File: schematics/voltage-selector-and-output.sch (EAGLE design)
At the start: 22 parts, among them IC1 3.3V, IC2 MIC2941, IC4 ULN2003AN, IC6 ATTINY85, IC7 74LS595N

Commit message: Finally updated the primary schematic
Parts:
- removed INPUT: (no value), SparkFun:M02PTH
- removed ISP1: AVRISP-6, adafruit:AVRISP-6
- removed JP1: (no value), SparkFun:M02JST-PTH-2
- removed R11: 10k, rcl-ez:R-US_0207/5V
- removed R7: 11k, rcl-ez:R-US_0207/5V
- removed R8: 20.5k, rcl-ez:R-US_0207/5V
- removed R9: 41.2k, rcl-ez:R-US_0207/5V
- removed R97: 6.49K 1%, rcl-ez:R-US_0207/5V
- added C1, C4: 47uF/25V, minimidi:CPOL-USE2.5-6
- added C5: 0.1uF, SparkFun-Capacitors:CAPPTH
- added D1, D2, D3, D4: 1N4007, gm-diodes:1N400X.3
- added D6: (no value), SparkFun-LED:LED-3MM-NO_SILK
- added IC3: MCP41010P, microchip-custom:MCP41010P
- added IC5: 12V, v-reg:78XXS
- added ISP: AVRISP-6, adafruit:AVRISP-6
- added JACK, XFRM: (no value), SparkFun:M02PTH
- added R2: 10k, rcl-ez:R-US_0207/5V
- added R3: 1K, rcl-ez:R-US_0207/5V
- added R4: 470, SparkFun-Resistors:RESISTORPTH-1/4W
- added TOGGLE: SPST, gm-switches:SPST
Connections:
- net N$17 renamed PB4
- removed net ISP_VCC: IC1.OUT, IC6.VCC, ISP1.VCC, JP4.1
- removed net N$15: IC6.PB5(NRES), ISP1.RST
- removed net N$16: IC6.PB3(ADC3), IC7A.SCK
- removed net N$18: IC6.PB2(SCK/ADC1), IC7A.RCK, ISP1.SCK
- removed net N$19: IC6.PB0(MOSI), ISP1.MOSI, JP4.2, R1.2
- removed net N$22: IC4.O1, R7.2
- removed net N$23: IC6.PB1(MISO), IC7A.SER, ISP1.MISO
- removed net N$24: IC4.O2, R8.2
- removed net N$25: IC4.O3, R9.2
- removed net N$8: IC2.ADJ, POT.2, R97.2
- new net IC_VCC: IC1.OUT, IC3.PA0, IC3.VDD, IC6.VCC, ISP.VCC, JP4.1
- new net N$2: D1.A, D3.C, XFRM.2
- new net N$3: D2.A, D4.C, XFRM.1
- new net N$4: IC2.ADJ, IC3.PW0, R3.2
- new net N$5: D6.C, R4.2
- new net N$6: POT.2
- new net N$9: C4.+, D1.C, D2.C, TOGGLE.P
- new net PB0: IC6.PB0(MOSI), ISP.MOSI, JP4.2, R1.2
- new net PB1: IC3.SI, IC6.PB1(MISO), IC7A.SER, ISP.RST
- new net PB2: IC3.SCK, IC6.PB2(SCK/ADC1), IC7A.RCK, ISP.SCK
- new net PB3: IC3./CS, IC6.PB3(ADC3), IC7A.SCK
- new net PB5: IC6.PB5(NRES), ISP.MISO
- new net RECTIFIED_12VCC: C1.+, C5.1, D6.A, IC1.IN, IC2.IN, IC5.OUT
- net AGND: now also C1.-, C4.-, C5.2, D3.A, D4.A, IC3.PB0, IC3.VSS, IC5.GND, ISP.GND, JACK.2, R2.2, R3.1, R4.1; no longer IC4.GND, INPUT.1, ISP1.GND, R11.2, R97.1
- net N$1: now also IC5.IN, TOGGLE.S; no longer IC1.IN, IC2.IN, INPUT.2
- net N$27: no longer IC4.I1
- net N$28: no longer IC4.I2
- net N$29: no longer IC4.I3
- net N$30: no longer IC4.I4
- net N$31: no longer IC4.I5
- net N$34: now also R2.1; no longer R11.1
- net VADJ: now also JACK.1
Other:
- moved on the sheet: IC1, IC4, IC6, IC7, JP4, METER, POSTS, POT, R1, SOCKET, USB

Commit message: Changed the pin being used for the pot SI
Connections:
- net PB1: no longer IC3.SI
- net PB5: now also IC3.SI
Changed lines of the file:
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@@
 <label x="33.02" y="83.82" size="1.778" layer="95"/>
+</segment>
+<segment>
+<pinref part="IC3" gate="P1" pin="SI"/>
+<wire x1="43.18" y1="139.7" x2="45.72" y2="139.7" width="0.1524" layer="91"/>
+<label x="45.72" y="139.7" size="1.778" layer="95"/>
 </segment>
 </net>
@@
 <label x="58.42" y="104.14" size="1.778" layer="95"/>
 </segment>
-<segment>
-<pinref part="IC3" gate="P1" pin="SI"/>
-<wire x1="43.18" y1="139.7" x2="45.72" y2="139.7" width="0.1524" layer="91"/>
-<label x="45.72" y="139.7" size="1.778" layer="95"/>
-</segment>
 </net>

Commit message: Resized board boundary to what I have room for and removed transistor array
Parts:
- removed IC4: ULN2003AN, uln-udn:ULN2003AN
- added Q1: 2N3906, transistor-pnp:2N3906
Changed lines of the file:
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@@
 <part name="GND8" library="supply1" deviceset="AGND" device="" value="GND"/>
 <part name="JP4" library="SparkFun" deviceset="M08" device="1X08"/>
-<part name="IC4" library="uln-udn" deviceset="ULN2003A" device="N"/>
 <part name="GND7" library="supply1" deviceset="AGND" device="" value="GND"/>
 <part name="IC7" library="74xx-us" deviceset="74*595" device="N" technology="LS"/>
@@
 <part name="C5" library="SparkFun-Capacitors" deviceset="CAP" device="PTH" value="0.1uF"/>
 <part name="JACK" library="SparkFun" deviceset="M02" device="PTH"/>
+<part name="Q1" library="transistor-pnp" deviceset="2N3906" device=""/>
 </parts>
 <sheets>
@@
 <instance part="GND8" gate="VR1" x="40.64" y="111.76" rot="R180"/>
 <instance part="JP4" gate="G$1" x="106.68" y="93.98" rot="MR0"/>
-<instance part="IC4" gate="A" x="124.46" y="213.36" rot="MR0"/>
 <instance part="GND7" gate="VR1" x="101.6" y="106.68" rot="MR180"/>
 <instance part="IC7" gate="A" x="73.66" y="93.98"/>
@@
 <instance part="C5" gate="G$1" x="88.9" y="223.52"/>
 <instance part="JACK" gate="G$1" x="132.08" y="134.62" rot="R180"/>
+<instance part="Q1" gate="G$1" x="78.74" y="119.38"/>
 </instances>
 <busses>

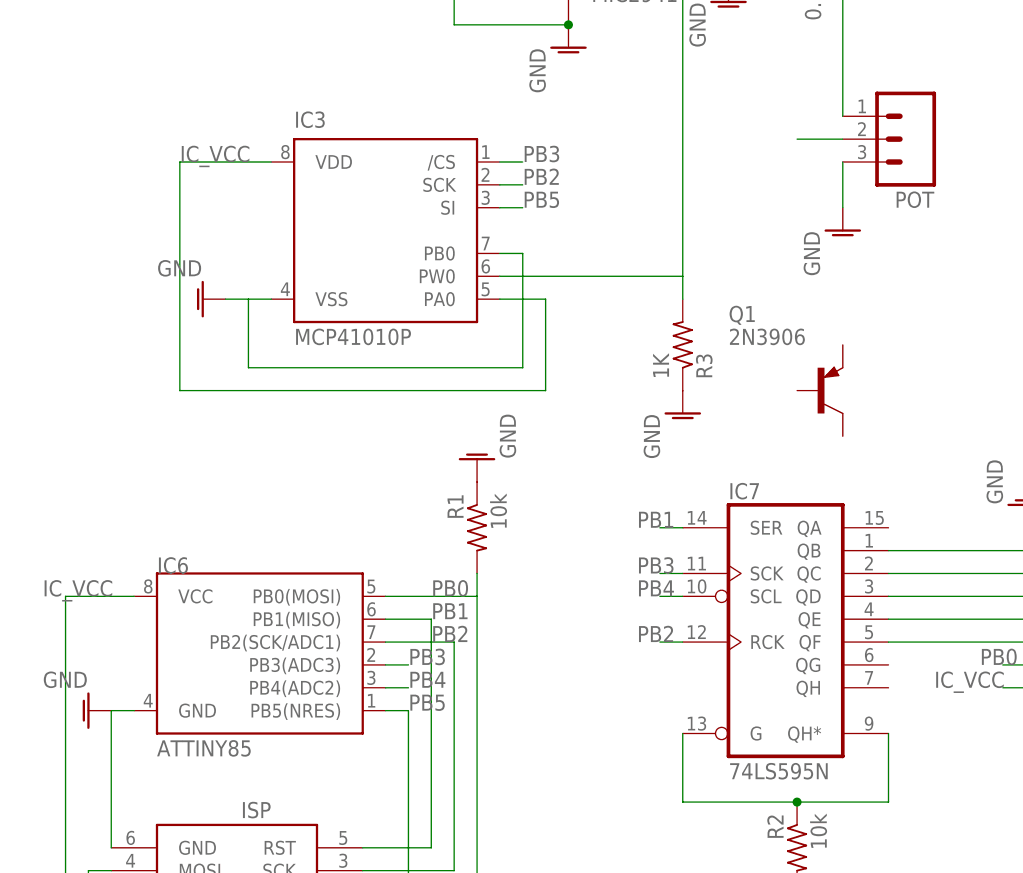
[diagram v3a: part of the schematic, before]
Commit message: Finally got to working on the main board layout
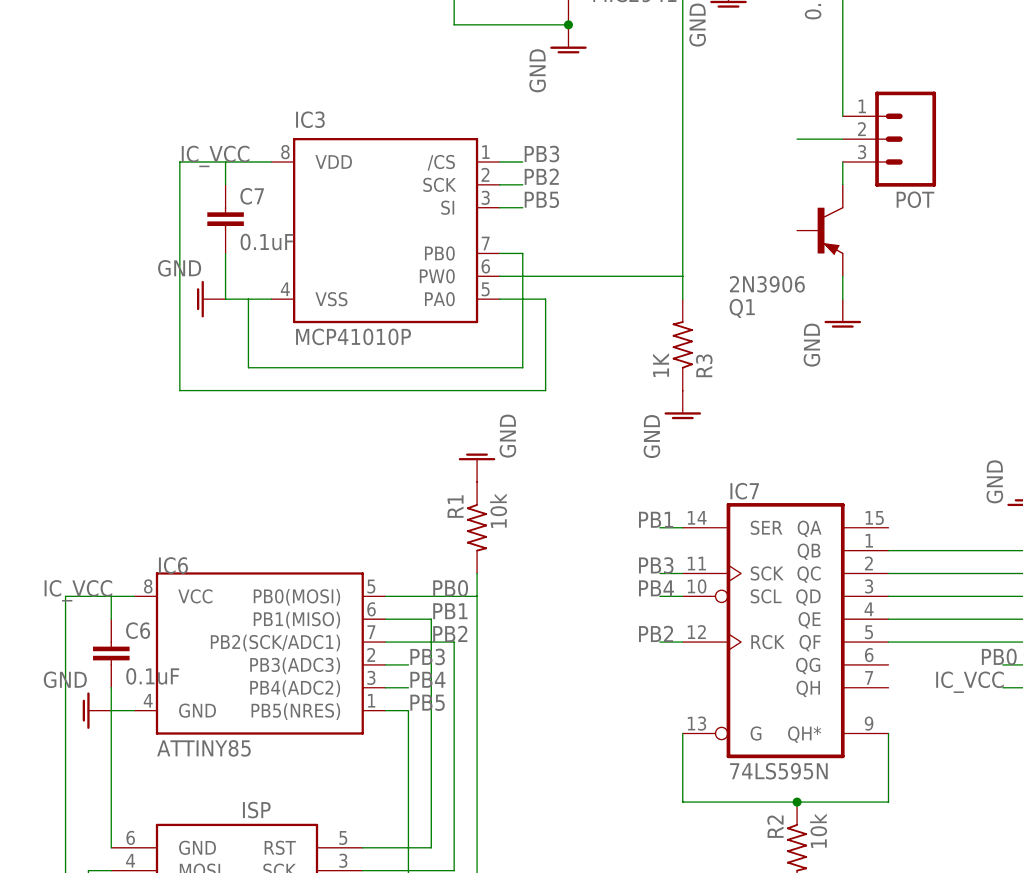
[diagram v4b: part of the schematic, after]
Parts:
- added C6, C7: 0.1uF, SparkFun-Capacitors:CAPPTH
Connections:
- new net N$7: POT.3, Q1.C
- net AGND: now also C6.2, C7.2, Q1.E; no longer POT.3
- net IC_VCC: now also C6.1, C7.1
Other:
- moved on the sheet: Q1
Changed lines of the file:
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@@
 <part name="JACK" library="SparkFun" deviceset="M02" device="PTH"/>
 <part name="Q1" library="transistor-pnp" deviceset="2N3906" device=""/>
+<part name="C6" library="SparkFun-Capacitors" deviceset="CAP" device="PTH" value="0.1uF"/>
+<part name="C7" library="SparkFun-Capacitors" deviceset="CAP" device="PTH" value="0.1uF"/>
 </parts>
 <sheets>
@@
 <instance part="USB" gate="G$1" x="132.08" y="172.72" rot="R180"/>
 <instance part="POT" gate="G$1" x="88.9" y="147.32" rot="R180"/>
-<instance part="GND11" gate="VR1" x="81.28" y="137.16"/>
+<instance part="GND11" gate="VR1" x="81.28" y="127"/>
 <instance part="IC3" gate="P1" x="30.48" y="137.16"/>
 <instance part="ISP" gate="G$1" x="15.24" y="66.04" rot="R180"/>
@@
 <instance part="C5" gate="G$1" x="88.9" y="223.52"/>
 <instance part="JACK" gate="G$1" x="132.08" y="134.62" rot="R180"/>
-<instance part="Q1" gate="G$1" x="78.74" y="119.38"/>
+<instance part="Q1" gate="G$1" x="78.74" y="137.16" rot="MR180"/>
+<instance part="C6" gate="G$1" x="0" y="88.9"/>
+<instance part="C7" gate="G$1" x="12.7" y="137.16"/>
 </instances>
 <busses>
@@
 <wire x1="0" y1="63.5" x2="-5.08" y2="63.5" width="0.1524" layer="91"/>
 <wire x1="-5.08" y1="63.5" x2="-5.08" y2="96.52" width="0.1524" layer="91"/>
-<wire x1="-5.08" y1="96.52" x2="2.54" y2="96.52" width="0.1524" layer="91"/>
+<wire x1="-5.08" y1="96.52" x2="0" y2="96.52" width="0.1524" layer="91"/>
+<pinref part="C6" gate="G$1" pin="1"/>
+<wire x1="0" y1="96.52" x2="2.54" y2="96.52" width="0.1524" layer="91"/>
+<wire x1="0" y1="93.98" x2="0" y2="96.52" width="0.1524" layer="91"/>
 </segment>
 <segment>
@@
 <wire x1="7.62" y1="119.38" x2="7.62" y2="144.78" width="0.1524" layer="91"/>
 <pinref part="IC3" gate="P1" pin="VDD"/>
-<wire x1="7.62" y1="144.78" x2="17.78" y2="144.78" width="0.1524" layer="91"/>
+<wire x1="7.62" y1="144.78" x2="12.7" y2="144.78" width="0.1524" layer="91"/>
 <label x="7.62" y="144.78" size="1.778" layer="95"/>
+<pinref part="C7" gate="G$1" pin="1"/>
+<wire x1="12.7" y1="144.78" x2="17.78" y2="144.78" width="0.1524" layer="91"/>
+<wire x1="12.7" y1="142.24" x2="12.7" y2="144.78" width="0.1524" layer="91"/>
 </segment>
 </net>
@@
 </segment>
 <segment>
-<pinref part="POT" gate="G$1" pin="3"/>
 <pinref part="GND11" gate="VR1" pin="AGND"/>
-<wire x1="81.28" y1="144.78" x2="81.28" y2="139.7" width="0.1524" layer="91"/>
+<pinref part="Q1" gate="G$1" pin="E"/>
+<wire x1="81.28" y1="132.08" x2="81.28" y2="129.54" width="0.1524" layer="91"/>
 </segment>
 <segment>
@@
 <wire x1="45.72" y1="121.92" x2="15.24" y2="121.92" width="0.1524" layer="91"/>
 <wire x1="15.24" y1="121.92" x2="15.24" y2="129.54" width="0.1524" layer="91"/>
+<pinref part="C7" gate="G$1" pin="2"/>
+<wire x1="12.7" y1="134.62" x2="12.7" y2="129.54" width="0.1524" layer="91"/>
 </segment>
 <segment>
@@
 <wire x1="0" y1="83.82" x2="2.54" y2="83.82" width="0.1524" layer="91"/>
 <wire x1="0" y1="68.58" x2="0" y2="83.82" width="0.1524" layer="91"/>
+<pinref part="C6" gate="G$1" pin="2"/>
+<wire x1="0" y1="86.36" x2="0" y2="83.82" width="0.1524" layer="91"/>
 </segment>
 <segment>
@@
 </segment>
 </net>
+<net name="N$7" class="0">
+<segment>
+<pinref part="POT" gate="G$1" pin="3"/>
+<wire x1="81.28" y1="144.78" x2="81.28" y2="142.24" width="0.1524" layer="91"/>
+<pinref part="Q1" gate="G$1" pin="C"/>
+</segment>
+</net>

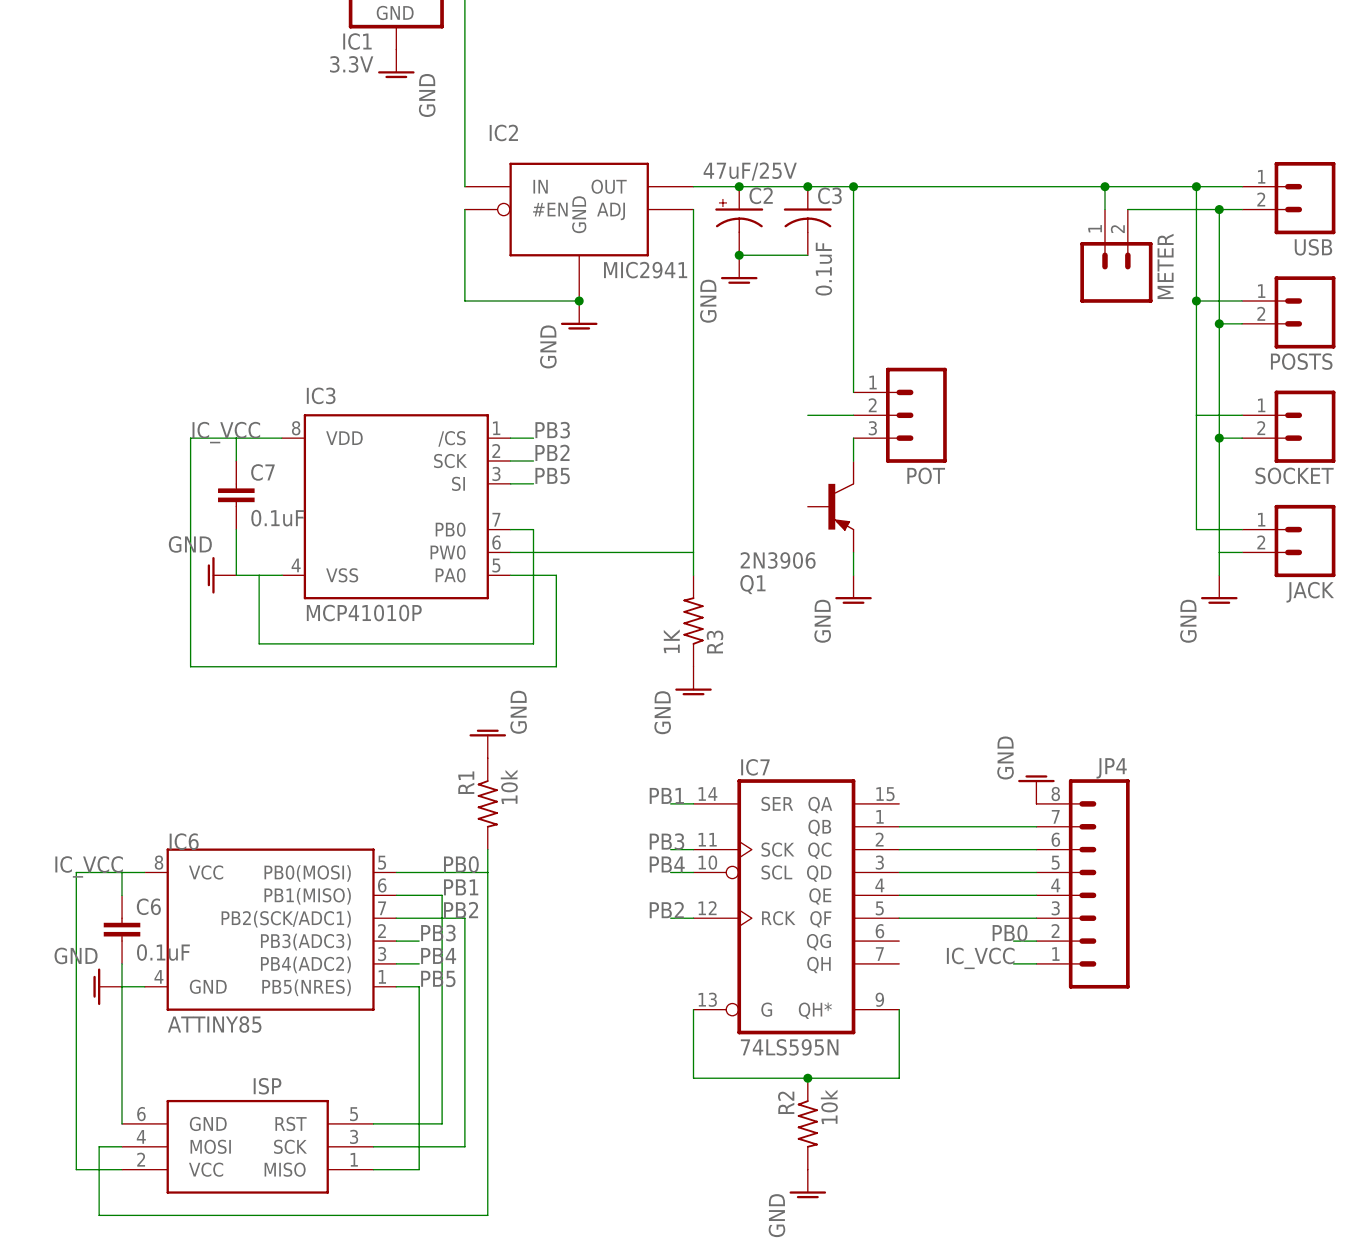
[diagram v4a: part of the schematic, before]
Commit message: Moved the shift register to the top board since I have more room there and on the bottom board and I get to free up some pins on the jumper
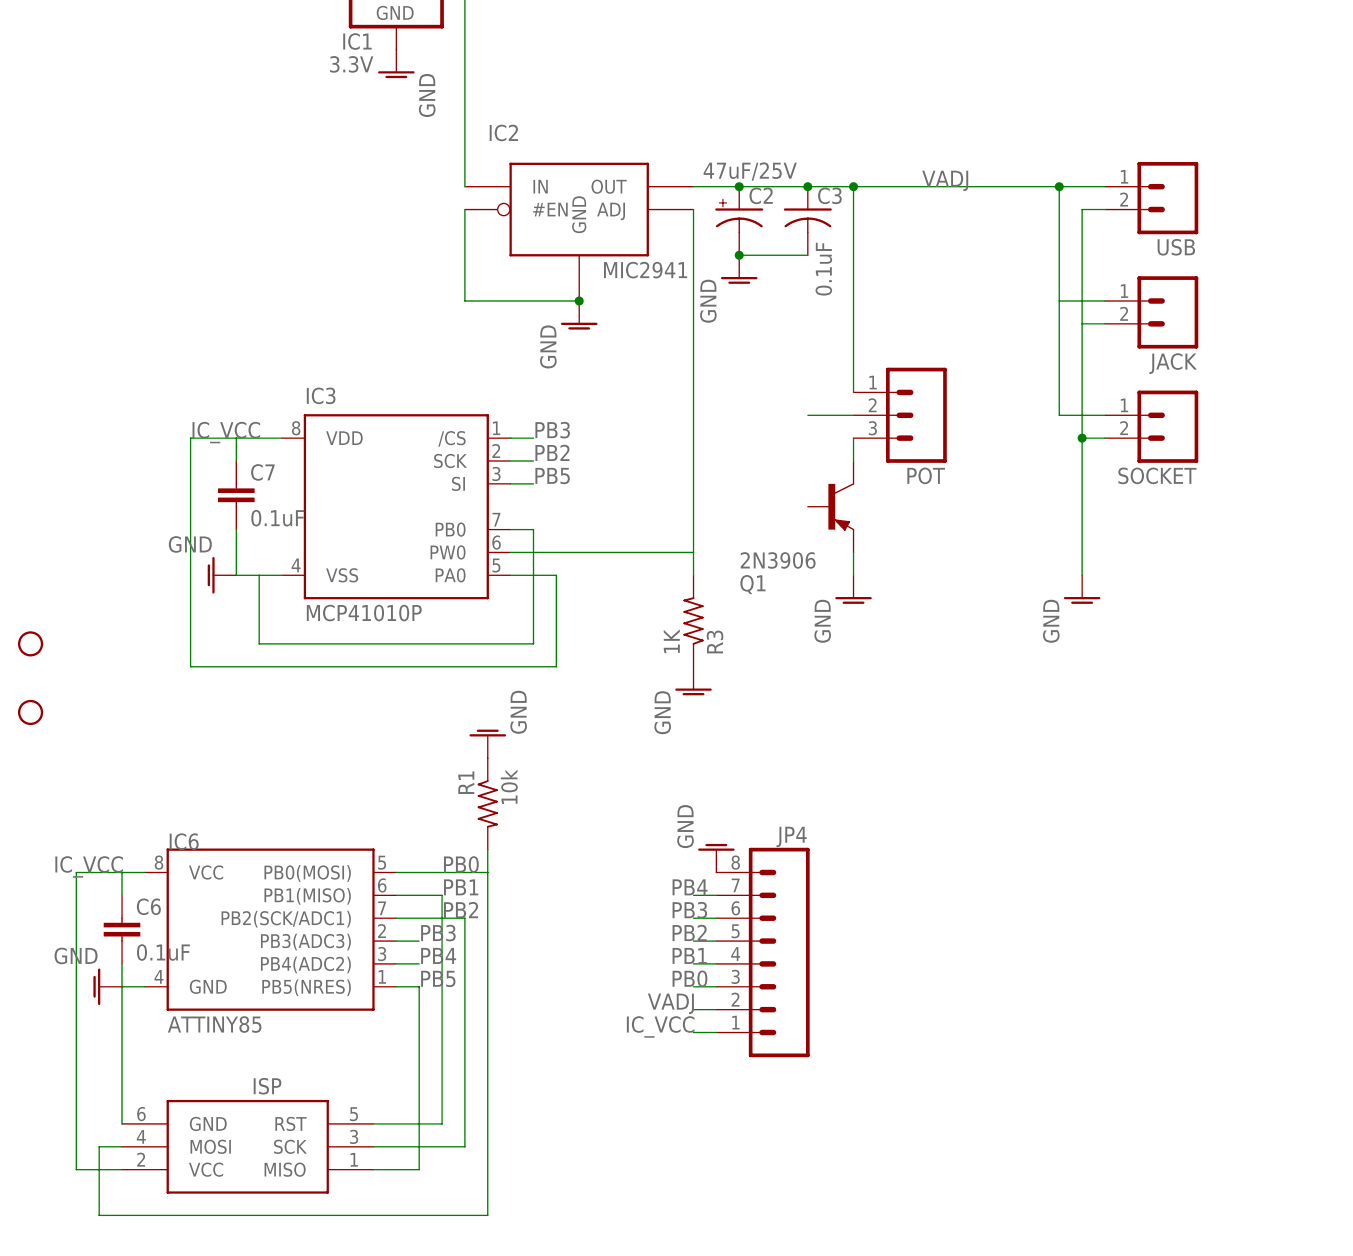
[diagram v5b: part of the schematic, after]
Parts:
- removed IC7: 74LS595N, 74xx-us:74LS595N
- removed METER, POSTS: (no value), SparkFun:M02PTH
- removed R2: 10k, rcl-ez:R-US_0207/5V
- added STANDOFF1, STANDOFF2: STAND-OFF, SparkFun-Electromechanical:STAND-OFF
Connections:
- removed net N$27: IC7A.QB, JP4.7
- removed net N$28: IC7A.QC, JP4.6
- removed net N$29: IC7A.QD, JP4.5
- removed net N$30: IC7A.QE, JP4.4
- removed net N$31: IC7A.QF, JP4.3
- removed net N$34: IC7A.G, IC7A.QH*, R2.1
- net AGND: no longer METER.2, POSTS.2, R2.2
- net PB0: now also JP4.3; no longer JP4.2
- net PB1: now also JP4.4; no longer IC7A.SER
- net PB2: now also JP4.5; no longer IC7A.RCK
- net PB3: now also JP4.6; no longer IC7A.SCK
- net PB4: now also JP4.7; no longer IC7A.SCL
- net VADJ: now also JP4.2; no longer METER.1, POSTS.1
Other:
- moved on the sheet: JACK, JP4, SOCKET, USB

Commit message: Doing this instead of working out. Yup
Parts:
- IC1: value 3.3V -> 5V
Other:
- moved on the sheet: C6, IC6, ISP, JP4, R1
